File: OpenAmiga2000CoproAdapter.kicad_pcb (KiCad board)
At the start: 2 copper layers, 188.6 x 114.2 mm, 76 parts, among them CN1 A2000_COPRO_SLOT, P1 CONN_2, P10 CONN_1, P11 CONN_1, P12 CONN_1, P13 CONN_1, P14 CONN_1, P15 CONN_1, P2 CONN_2, P3 CONN_2, P4 CONN_2, P5 CONN_1, P6 CONN_1, P7 CONN_1, P8 CONN_1, P9 CONN_1, P99 OSHW_LOGO, U1 68000D, U10 Spare, U11 74HCT00, U12 74HCT27, U13 74HCT74, U14 74F86, U15 74F74, U16 74HCT04, U17 74HCT112, U18 74F157, U19 74F157, U2 AS6C4008-55PCN, U3 AS6C4008-55PCN, U4 AS6C4008-55PCN, U5 AS6C4008-55PCN, U6 74HCT00, U7 74HCT32, U8 74HCT32, U9 74LS05

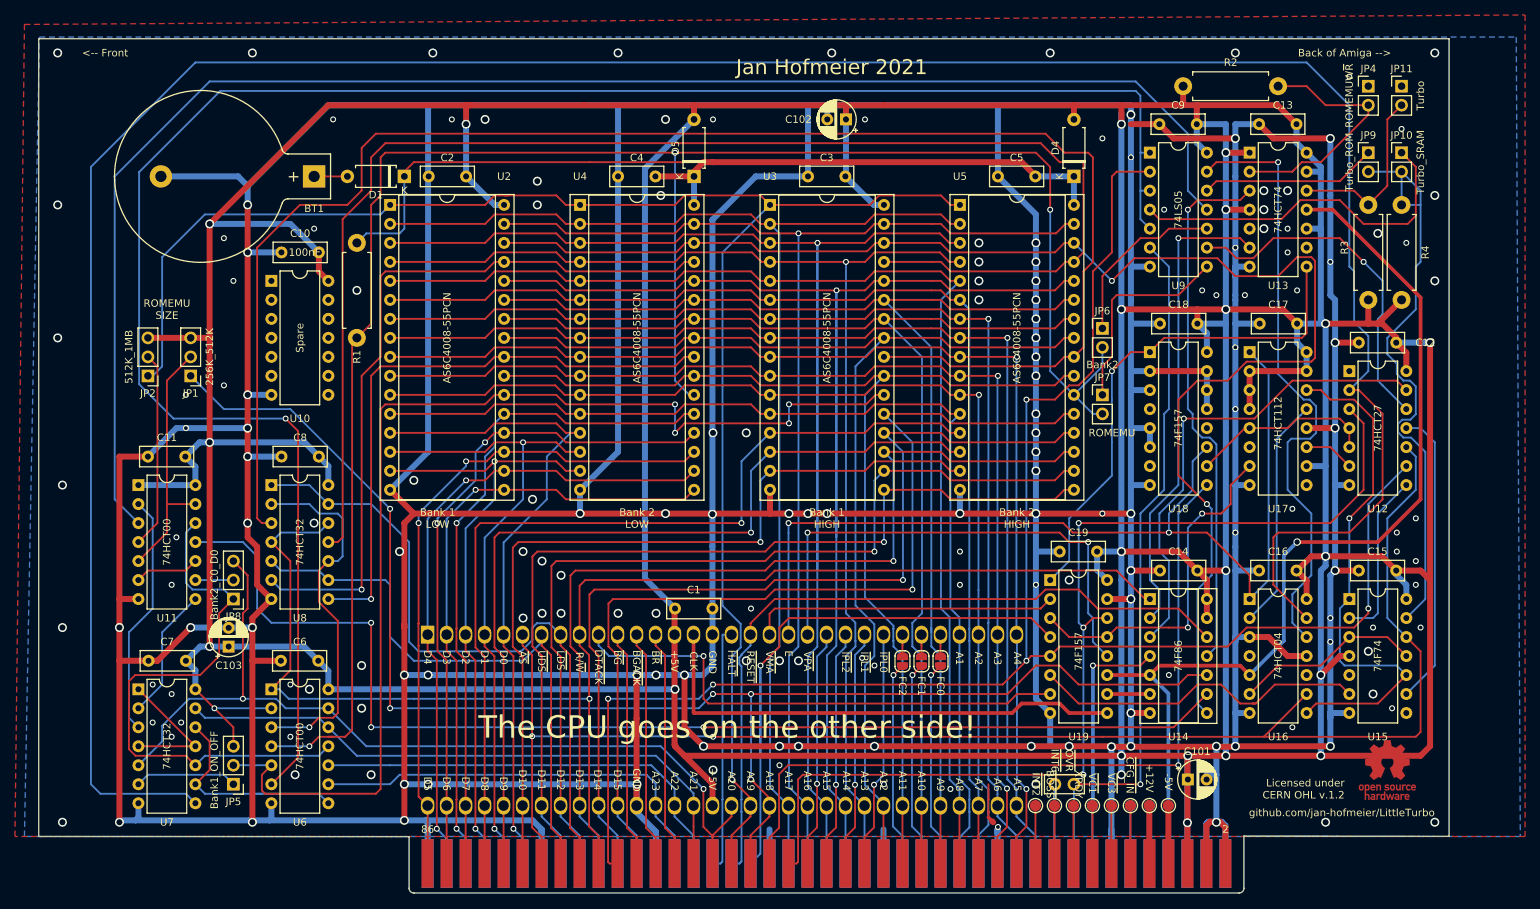
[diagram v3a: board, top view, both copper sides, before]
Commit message: dont mirror in lower 512k
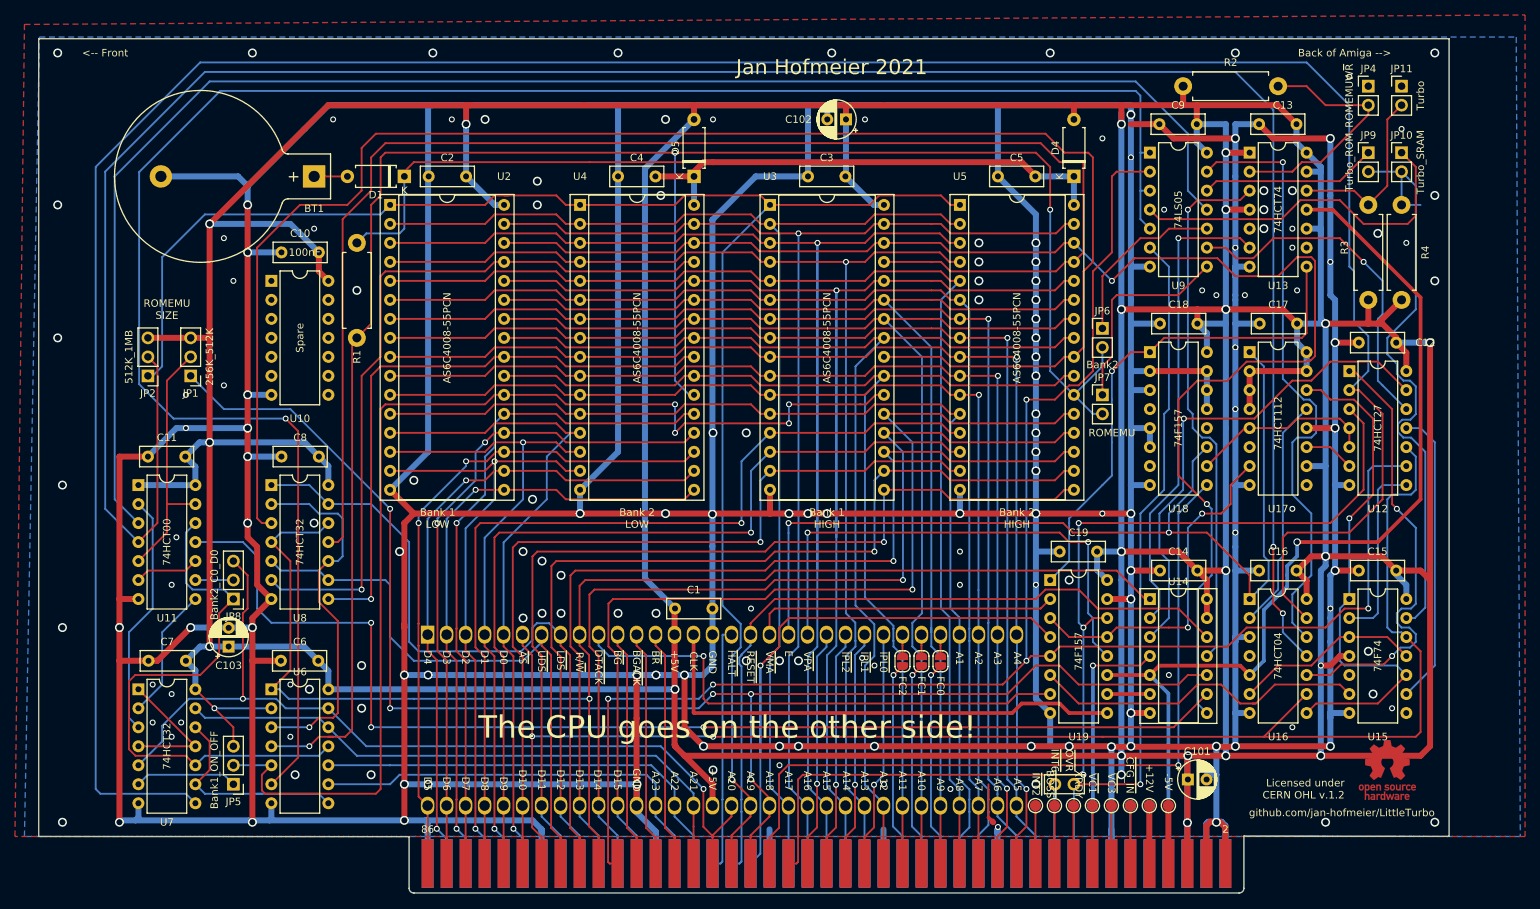
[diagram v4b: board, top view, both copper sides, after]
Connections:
- U12 pad 1: GND -> Net-(U12-Pad1)
- U16 pad 10: Net-(U16-Pad10) -> Net-(U12-Pad1)
- U16 pad 11: GND -> Net-(JP2-Pad2)
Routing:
- net Net-(JP2-Pad2): track 26.3 -> 316.4 mm, vias 0 -> 2
- net Net-(U12-Pad1): track 0.00 -> 61.0 mm, vias 0 -> 2
- net GND: track 1472.6 -> 1463.0 mm, vias 180 -> 172
- net /Memory/~ROMEN: track 360.7 -> 358.0 mm
- net /~dtack: track 229.2 -> 231.4 mm
- net /~as: track 200.9 -> 203.1 mm
- net Net-(U12-Pad13): track 64.5 -> 66.6 mm
- net Net-(U12-Pad8): track 22.8 -> 24.7 mm
- net +5V: track 1119.6 -> 1119.1 mm
- net Net-(U16-Pad12): track 82.3 -> 81.8 mm

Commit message: fix connector and small stuff
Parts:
- moved P99 196.0 mm to (47.6, 40.0)
- moved C103 0.63 mm to (67.2, 113.7)
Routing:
- net +5V: track 1119.1 -> 1114.5 mm
- net GND: track 1463.0 -> 1461.9 mm, vias 172 -> 181
- net /~dtack: track 231.4 -> 230.8 mm
- net /~vpa: track 140.0 -> 139.3 mm
- net /~rst: track 99.6 -> 99.0 mm

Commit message: visuals
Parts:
- moved JP1 0.63 mm to (60.9, 77.5)
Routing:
- net /a18: track 198.6 -> 199.3 mm
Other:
- board text added: "Based on work by Kipper2K, SukkoPera, Livio Plos and Jörg Richter"

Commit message: update routes
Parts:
- removed JP7: ROMEMU, Connector_PinHeader_2.54mm:PinHeader_1x02_P2.54mm_Vertical
- removed R2: 500, Resistor_THT:R_Axial_DIN0411_L9.9mm_D3.6mm_P12.70mm_Horizontal
- added JP3: Bank2, Connector_PinHeader_2.54mm:PinHeader_1x02_P2.54mm_Vertical, F.Cu at (183.5, 71.1)
- JP2: value 512K_1MB -> 1MB_512K
- JP4: value ROMEMUW~R -> ROM_R_W; footprint Connector_PinHeader_2.54mm:PinHeader_1x02_P2.54mm_Vertical -> Connector_PinHeader_2.54mm:PinHeader_1x03_P2.54mm_Vertical
- JP6: value Bank2 -> Mirror_OFF_ON; footprint Connector_PinHeader_2.54mm:PinHeader_1x02_P2.54mm_Vertical -> Connector_PinHeader_2.54mm:PinHeader_1x03_P2.54mm_Vertical
- JP8: value Bank2_C0_D0 -> Bank2 D0_C0
- moved JP6 117.5 mm to (66.0, 72.4)
- moved JP1 5.08 mm to (60.9, 72.4), turned to 0 degrees
- moved JP2 5.08 mm to (55.8, 72.4), turned to 0 degrees
- moved JP8 5.08 mm to (67.2, 102.2), turned to 0 degrees
- moved JP4 1.27 mm to (219.0, 37.5)
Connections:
- net /Memory/ROM~R~W renamed /Memory/ROMR~W
- JP1 pad 1: /a18 -> GND
- JP2 pad 1: /a19 -> GND
- JP2 pad 3: +5V -> Net-(JP2-Pad3)
- JP4 pad 1: GND -> +5V
- JP6 pad 1: Net-(JP6-Pad1) -> /a18
- JP6 pad 2: /Memory/~CS2 -> /Memory/a18m
- JP8 pad 1: Net-(JP8-Pad1) -> /a20
- JP8 pad 2: Net-(JP8-Pad2) -> Net-(JP2-Pad3)
- JP8 pad 3: /a20 -> Net-(JP8-Pad3)
- JP9 pad 1: Net-(JP9-Pad1) -> /Memory/~ROMEN
- U11 pad 1: +5V -> /Memory/ROMEN
- U11 pad 11: Net-(U11-Pad11) -> Net-(U11-Pad10)
- U11 pad 12: Net-(JP8-Pad1) -> /a19
- U11 pad 2: Net-(U11-Pad2) -> /Memory/SROMON
- U11 pad 3: /Memory/CSRAM2 -> /Memory/~SROM
- U11 pad 4: Net-(JP2-Pad2) -> /Memory/~SROM
- U11 pad 5: Net-(JP1-Pad2) -> /Memory/~RAM2
- U11 pad 6: Net-(U11-Pad10) -> Net-(U11-Pad6)
- U11 pad 9: Net-(JP8-Pad2) -> Net-(JP2-Pad2)
- U12 pad 1: Net-(U12-Pad1) -> /Memory/~HIGH
- U12 pad 12: /Memory/CSROM -> /Memory/ROMEN
- U12 pad 2: /Memory/~ROMEN -> /Memory/~a21
- U13 pad 6: Net-(U13-Pad6) -> (no net)
- U13 pad 9: Net-(U13-Pad9) -> (no net)
- U14 pad 10: /a18 -> GND
- U14 pad 11: Net-(U13-Pad3) -> Net-(U12-Pad13)
- U14 pad 12: /~rst -> /a19
- U14 pad 13: +5V -> /a20
- U14 pad 2: Net-(U13-Pad6) -> Net-(U13-Pad5)
- U14 pad 3: Net-(U12-Pad13) -> /Memory/SROMON
- U14 pad 8: /Memory/a18m -> (no net)
- U14 pad 9: Net-(U11-Pad11) -> GND
- U15 pad 5: Net-(U15-Pad5) -> (no net)
- U15 pad 8: Net-(U15-Pad8) -> (no net)
- U16 pad 10: Net-(U12-Pad1) -> (no net)
- U16 pad 11: Net-(JP2-Pad2) -> GND
- U16 pad 12: Net-(U16-Pad12) -> /Memory/~a21
- U16 pad 13: /Memory/~ROMEN -> /a21
- U16 pad 3: GND -> /~rst
- U16 pad 4: Net-(U16-Pad4) -> Net-(U13-Pad3)
- U17 pad 6: Net-(U17-Pad6) -> (no net)
- U17 pad 9: Net-(U17-Pad9) -> (no net)
- U18 pad 12: Net-(U18-Pad12) -> (no net)
- U18 pad 4: Net-(U18-Pad4) -> (no net)
- U18 pad 7: Net-(U18-Pad7) -> (no net)
- U6 pad 1: /r_~w -> /a20
- U6 pad 11: Net-(JP8-Pad1) -> /Memory/~OE
- U6 pad 12: /a21 -> /r_~w
- U6 pad 13: /a20 -> +5V
- U6 pad 3: /Memory/OE -> Net-(JP8-Pad3)
- U6 pad 8: Net-(U6-Pad8) -> /Memory/~HIGH
- U7 pad 1: /Memory/~CRAM -> Net-(U11-Pad8)
- U7 pad 10: Net-(JP8-Pad1) -> /a20
- U7 pad 11: /Memory/~CRAM -> Net-(JP6-Pad3)
- U7 pad 12: Net-(U6-Pad8) -> /Memory/~a21
- U7 pad 13: /a21 -> /a18
- U7 pad 2: Net-(U11-Pad8) -> /Memory/~CRAM
- U7 pad 3: Net-(U11-Pad2) -> /Memory/~RAM2
- U7 pad 4: /Memory/~CRAM -> /a21
- U7 pad 5: /a20 -> /Memory/~HIGH
- U7 pad 6: Net-(JP5-Pad1) -> /Memory/~CRAM
- U7 pad 8: /Memory/~ROMEN -> Net-(JP5-Pad1)
- U7 pad 9: Net-(U6-Pad8) -> /Memory/~CRAM
- U8 pad 10: /Memory/OE -> /Memory/~OE
- U8 pad 2: /Memory/OE -> /Memory/~OE
- U9 pad 10: Net-(JP6-Pad1) -> Net-(JP3-Pad1)
- U9 pad 11: /Memory/CSRAM2 -> Net-(U11-Pad6)
- U9 pad 12: Net-(JP9-Pad1) -> /Memory/~ROMEN
- U9 pad 13: Net-(U16-Pad12) -> /Memory/ROMEN
- U9 pad 2: /~dtack -> Net-(JP10-Pad1)
- U9 pad 4: Net-(JP10-Pad1) -> /~dtack
- U9 pad 8: Net-(JP7-Pad1) -> (no net)
- U9 pad 9: /Memory/CSROM -> GND
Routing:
- net /Memory/~ROMEN: track 358.0 -> 23.7 mm
- net Net-(JP2-Pad2): track 316.4 -> 32.5 mm, vias 2 -> 0
- net /Memory/~HIGH: track 0.00 -> 264.3 mm, vias 0 -> 4
- net /Memory/ROMEN: track 0.00 -> 256.7 mm, vias 0 -> 1
- net Net-(U11-Pad6): track 0.00 -> 224.8 mm
- net /Memory/CSRAM2: track 210.5 -> 0.00 mm
- net /Memory/~a21: track 0.00 -> 205.6 mm, vias 0 -> 4
- net /Memory/SROMON: track 0.00 -> 192.8 mm, vias 0 -> 4
- net Net-(U11-Pad11): track 159.6 -> 0.00 mm, vias 3 -> 0
- net /a21: track 80.7 -> 197.2 mm, vias 0 -> 1
- net /a20: track 120.7 -> 207.5 mm, vias 2 -> 4
- net /a19: track 224.7 -> 311.3 mm, vias 1 -> 2
- net Net-(U16-Pad12): track 81.8 -> 0.00 mm, vias 1 -> 0
- net Net-(JP8-Pad1): track 75.3 -> 0.00 mm
- net Net-(U13-Pad6): track 63.5 -> 0.00 mm, vias 1 -> 0
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
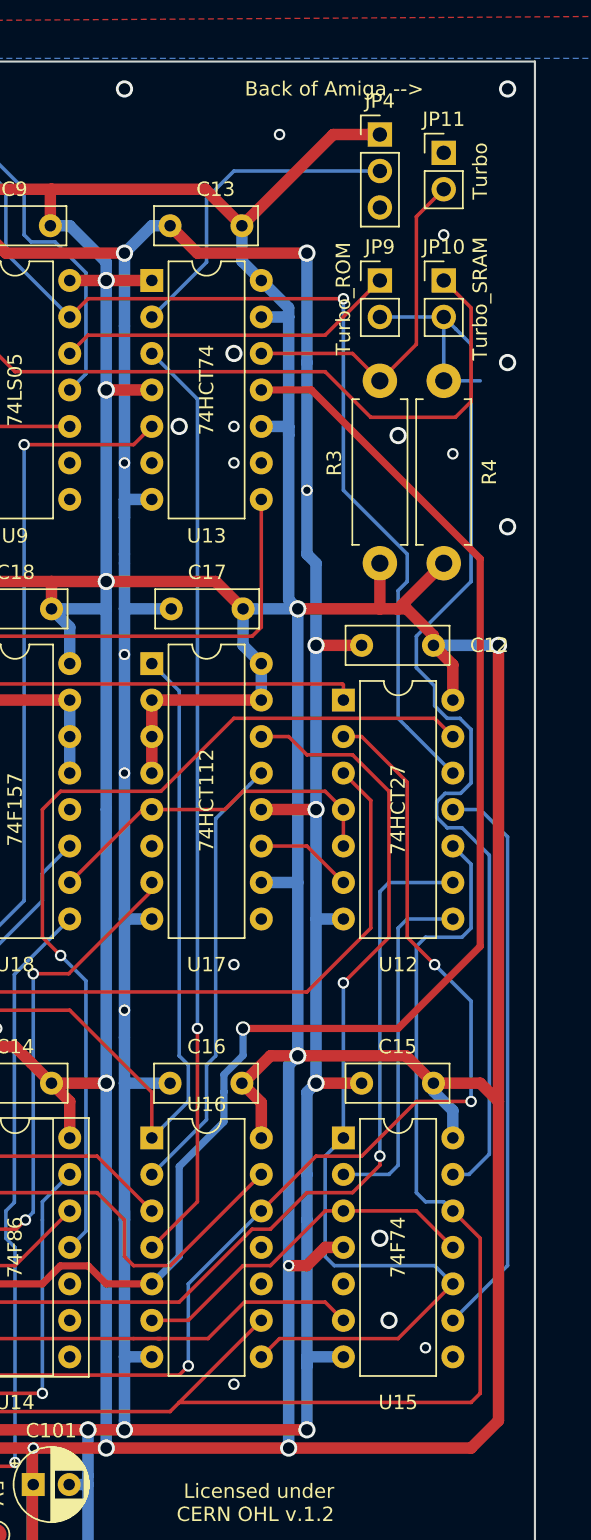
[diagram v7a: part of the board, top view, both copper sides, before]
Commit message: reorganize turbo jumpers
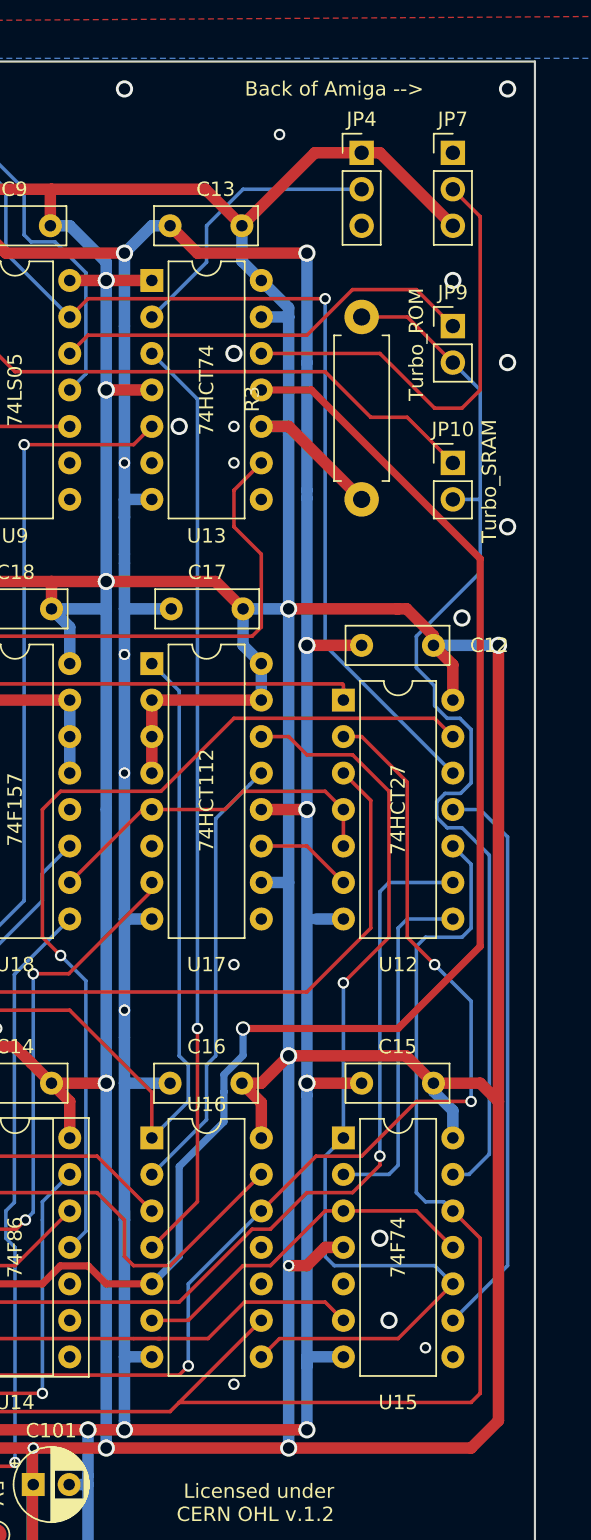
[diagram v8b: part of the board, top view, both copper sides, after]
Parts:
- removed JP11: Turbo, Connector_PinHeader_2.54mm:PinHeader_1x02_P2.54mm_Vertical
- removed R4: 500, Resistor_THT:R_Axial_DIN0411_L9.9mm_D3.6mm_P12.70mm_Horizontal
- added JP7: Turbo, Connector_PinHeader_2.54mm:PinHeader_1x03_P2.54mm_Vertical, F.Cu at (224.1, 38.7)
- moved JP10 12.7 mm to (224.1, 60.3)
- moved R3 7.24 mm to (217.7, 62.9)
- moved JP9 5.99 mm to (224.1, 50.8)
- moved JP4 1.80 mm to (217.7, 38.7)
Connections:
- U13 pad 8: Net-(U13-Pad8) -> (no net)
- U13 pad 9: (no net) -> Net-(U13-Pad9)
- U18 pad 1: Net-(U13-Pad8) -> Net-(U13-Pad9)
- U19 pad 1: Net-(U13-Pad8) -> Net-(U13-Pad9)
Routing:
- net Net-(U13-Pad9): track 0.00 -> 72.5 mm, vias 0 -> 1
- net Net-(U13-Pad8): track 68.4 -> 0.00 mm, vias 1 -> 0
- net Net-(JP10-Pad1): track 48.1 -> 38.5 mm
- net Net-(JP7-Pad2): track 24.2 -> 32.1 mm
- net +5V: track 1114.4 -> 1121.9 mm
- net /Memory/~ROMEN: track 23.7 -> 30.8 mm
- net /Memory/~DTACK_FAST: track 81.0 -> 76.3 mm
- net /Memory/ROMR~W: track 22.7 -> 19.8 mm
- net /Memory/ROMEN: track 256.7 -> 255.5 mm
- net GND: track 1463.8 -> 1463.5 mm, vias 137 -> 135
